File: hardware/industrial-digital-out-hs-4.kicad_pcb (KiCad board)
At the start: 2 copper layers, 40 x 40 mm, 40 parts, among them P1 CON-SENSOR, P2 Digital Output, P3 Debug, P4 Boot, Q1 FDS8449, U1 XMC1100, U2 VN7140AS, U3 VN7140AS, U4 VN7140AS, U5 VN7140AS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

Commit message: updated pcb design
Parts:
- moved R1 93.2 mm to (149.5, 88.3), turned to 90 degrees
- moved RP1 89.6 mm to (152.9, 88.2)
- moved C2 86.9 mm to (131.6, 77.9), turned to 180 degrees
- moved R2 85.6 mm to (143.5, 88.3), turned to 90 degrees
- moved RP4 82.3 mm to (146.9, 88.2)
- moved D5 81.9 mm to (150.8, 75.0), turned to 270 degrees
- moved P3 81.6 mm to (124.0, 85.2)
- moved RP2 81.0 mm to (131.6, 79.6), turned to 90 degrees
- moved R6 79.6 mm to (141.4, 94.6), turned to 90 degrees
- moved R7 77.0 mm to (141.4, 91.7), turned to 90 degrees
- moved D6 76.9 mm to (120.1, 91.6), turned to 270 degrees
- moved RP5 76.8 mm to (139.1, 88.2)
- moved RP3 76.5 mm to (148.4, 79.2), turned to 180 degrees
- moved D4 75.4 mm to (149.2, 75.0), turned to 270 degrees
- moved C3 74.1 mm to (139.4, 79.0)
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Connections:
- RP1 pad 1: OUT4 -> MSense4
- RP1 pad 4: MSense4 -> OUT4
- RP1 pad 5: Net-(R1-Pad1) -> Net-(RP1-Pad5)
- RP1 pad 8: Net-(RP1-Pad8) -> Net-(R1-Pad1)
- RP4 pad 1: OUT3 -> MSense3
- RP4 pad 4: MSense3 -> OUT3
- RP4 pad 5: Net-(R2-Pad1) -> Net-(RP4-Pad5)
- RP4 pad 8: Net-(RP4-Pad8) -> Net-(R2-Pad1)
- RP5 pad 1: OUT2 -> MSense2
- RP5 pad 4: MSense2 -> OUT2
- RP5 pad 5: Net-(R3-Pad1) -> Net-(RP5-Pad5)
- RP5 pad 8: Net-(RP5-Pad8) -> Net-(R3-Pad1)
- RP6 pad 1: OUT1 -> MSense1
- RP6 pad 4: MSense1 -> OUT1
- RP6 pad 5: Net-(R4-Pad1) -> Net-(RP6-Pad5)
- RP6 pad 8: Net-(RP6-Pad8) -> Net-(R4-Pad1)
- U1 pad 11: Net-(P4-Pad2) -> (no net)
- U1 pad 12: Net-(R5-Pad1) -> Net-(P4-Pad2)
- U1 pad 15: OUT4 -> OUT2
- U1 pad 17: OUT2 -> OUT4
- U1 pad 2: (no net) -> Net-(R5-Pad1)
- U1 pad 5: MSense2 -> VSense2
- U1 pad 6: MSense1 -> MSense2
- U1 pad 7: VSense2 -> MSense1
- U2 pad 1: Net-(RP1-Pad8) -> Net-(RP1-Pad5)
- U3 pad 1: Net-(RP4-Pad8) -> Net-(RP4-Pad5)
- U4 pad 1: Net-(RP5-Pad8) -> Net-(RP5-Pad5)
- U5 pad 1: Net-(RP6-Pad8) -> Net-(RP6-Pad5)
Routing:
- net 3V3: track 0.00 -> 98.5 mm
- net MSense4: track 0.00 -> 34.0 mm, vias 0 -> 2
- net VSense2: track 0.00 -> 33.4 mm, vias 0 -> 2
- net GND: track 0.00 -> 33.4 mm, vias 9 -> 32
- net OUT4: track 0.00 -> 31.5 mm
- net MSense3: track 0.00 -> 28.8 mm, vias 0 -> 2
- net OUT3: track 0.00 -> 26.0 mm
- net LED3: track 0.00 -> 25.0 mm
- net LED2: track 0.00 -> 23.4 mm
- net LED1: track 0.00 -> 22.5 mm
- net MSense2: track 0.00 -> 22.4 mm, vias 0 -> 2
- net LED0: track 0.00 -> 21.5 mm
- net VSense1: track 0.00 -> 20.9 mm, vias 0 -> 2
- net OUT2: track 0.00 -> 18.7 mm
- net MSense1: track 0.00 -> 16.8 mm, vias 0 -> 2
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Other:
- rule trace_min: 0.1 -> 0.15
- board text added: "0"
- board text added: "1"
- board text added: "2"
- board text added: "3"
- board text added: "Status"

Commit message: first finished prototype design
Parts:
- added Fiducial_Mark: VAL**, kicad-libraries:Fiducial_Mark, F.Cu at (155.0, 81.0)
- added Fiducial_Mark: VAL**, kicad-libraries:Fiducial_Mark, F.Cu at (120.0, 87.0)
- added Fiducial_Mark: VAL**, kicad-libraries:Fiducial_Mark, F.Cu at (155.0, 105.0)
- added Fiducial_Mark: VAL**, kicad-libraries:Fiducial_Mark, F.Cu at (142.5, 86.5)
- added Fiducial_Mark: VAL**, kicad-libraries:Fiducial_Mark, F.Cu at (125.5, 111.0)
- added G***: LOGO, kicad-libraries:Logo_CoMCU, B.Cu at (145.0, 93.0)
- added G***: LOGO, kicad-libraries:Logo_31x31, F.Cu at (144.4, 82.2)
- added VAL: WEEE_7mm, kicad-libraries:WEEE_7mm, B.Cu at (138.0, 93.0)
- added VAL: CE_5mm, kicad-libraries:CE_5mm, B.Cu at (131.5, 93.0)
- moved C1 0.71 mm to (139.8, 81.2)
- moved C2 0.71 mm to (132.1, 78.4)
- moved C3 0.71 mm to (139.9, 79.5)
- moved C4 0.71 mm to (121.9, 82.2)
- moved D1 0.71 mm to (129.5, 75.5)
- moved D2 0.71 mm to (146.5, 75.5)
- moved D3 0.71 mm to (148.1, 75.5)
- moved D4 0.71 mm to (149.7, 75.5)
- moved D5 0.71 mm to (151.3, 75.5)
- moved D6 0.71 mm to (120.6, 92.1)
- moved P1 0.71 mm to (138.0, 73.0)
- moved P2 0.71 mm to (138.0, 104.9)
- moved P3 0.71 mm to (124.5, 85.7)
- moved Q1 0.71 mm to (124.1, 94.9)
- moved R1 0.71 mm to (150.0, 88.8)
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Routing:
- net GND: track 33.4 -> 34.9 mm
- net VSense1: track 20.9 -> 22.2 mm
- net Net-(P4-Pad2): track 2.54 -> 3.05 mm
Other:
- net class Default: clearance 0.2 -> 0.19
- rule trace_clearance: 0.2 -> 0.19
- board text added: "1+2"
- board text added: "3+4"
- board text added: "4"
- board text added: "ANPASSEN!"
- board text added: "GND"
- board text added: "Industrial Digital Out HS 4"
- board text added: "OUT"
- board text added: "VCC"
- board text added: "max. 26VDC"
- board text added: "max. 4 x ?A"
- board text added: "tinkerforge.com"

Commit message: drc check
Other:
- net class Default: clearance 0.19 -> 0.149
- rule pad_to_mask_clearance: 0.051 -> 0
- rule trace_clearance: 0.19 -> 0.149
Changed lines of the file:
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@@
     (user_trace_width 2)
     (user_trace_width 3)
-    (trace_clearance 0.19)
+    (trace_clearance 0.149)
     (zone_clearance 0.2)
     (zone_45_only no)
@@
     (pad_size 1.4 1.4)
     (pad_drill 0.6)
-    (pad_to_mask_clearance 0.051)
-    (solder_mask_min_width 0.25)
+    (pad_to_mask_clearance 0)
     (aux_axis_origin 118 73)
     (grid_origin 118 73)
@@
     (pcbplotparams
       (layerselection 0x010fc_ffffffff)
-      (usegerberextensions false)
+      (usegerberextensions true)
       (usegerberattributes false)
       (usegerberadvancedattributes false)
@@
       (plotinvisibletext false)
       (padsonsilk false)
-      (subtractmaskfromsilk false)
+      (subtractmaskfromsilk true)
       (outputformat 1)
       (mirror false)
-      (drillshape 1)
+      (drillshape 0)
       (scaleselection 1)
-      (outputdirectory ""))
+      (outputdirectory "proto/"))
   )
   (net 0 "")
@@
   (net 52 "Net-(RP5-Pad5)")
   (net_class Default "Dies ist die voreingestellte Netzklasse."
-    (clearance 0.19)
+    (clearance 0.149)
     (trace_width 0.25)
     (via_dia 0.8)
@@
       (pts
         (xy 141.6 102.7) (xy 139.2 102.7) (xy 138 103.6) (xy 138 112.55) (xy 123.5 112.55)
-        (xy 123.5 107.4) (xy 134.7 107.4) (xy 134.7 103.5) (xy 135.2 91.8) (xy 141.6 91.8)
+        (xy 123.5 107.4) (xy 134.7 107.4) (xy 134.7 103.5) (xy 134.7 91.8) (xy 141.6 91.8)
       )
     )
@@
     (polygon
       (pts
-        (xy 149.2 91.8) (xy 155.6 91.8) (xy 155.6 102.7) (xy 153.2 102.7) (xy 152.3 103.6)
+        (xy 148.7 91.8) (xy 155.6 91.8) (xy 155.6 102.7) (xy 153.2 102.7) (xy 152.3 103.6)
         (xy 152.3 107) (xy 148.7 107) (xy 148.7 103.5)
       )

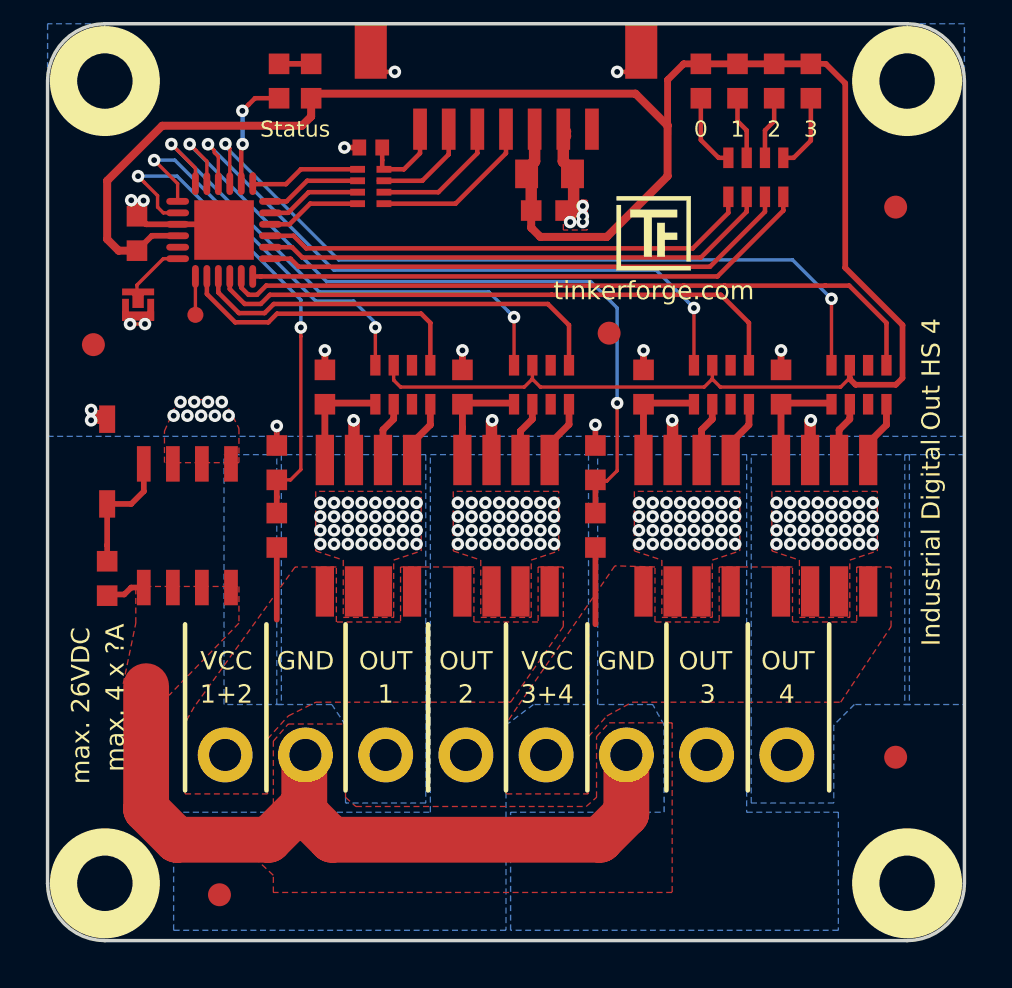
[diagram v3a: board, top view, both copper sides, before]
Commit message: changed out pins to enable pwm, changed pcb design, plotted gerber files for prototype
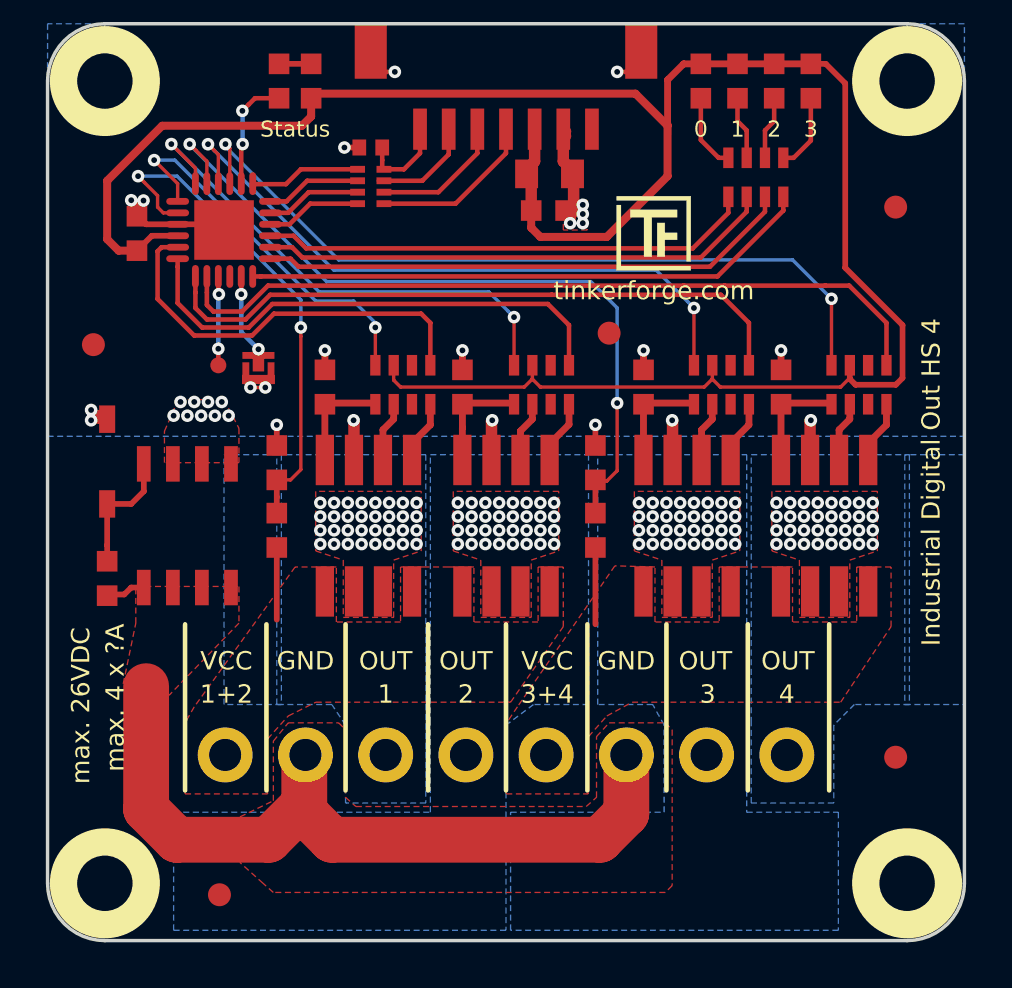
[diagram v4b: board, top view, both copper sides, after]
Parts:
- moved P4 5.94 mm to (127.2, 88.0)
- moved P3 2.42 mm to (125.5, 87.9)
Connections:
- P1 pad 1: (no net) -> Net-(P1-Pad1)
- R6 pad 2: VSense2 -> VSense1
- R7 pad 1: VSense2 -> VSense1
- R8 pad 2: VSense1 -> VSense0
- R9 pad 1: VSense1 -> VSense0
- RP1 pad 1: MSense4 -> MSense3
- RP1 pad 3: (no net) -> Net-(RP1-Pad3)
- RP1 pad 4: OUT4 -> OUT3
- RP1 pad 6: (no net) -> Net-(RP1-Pad6)
- RP4 pad 1: MSense3 -> MSense2
- RP4 pad 3: (no net) -> Net-(RP4-Pad3)
- RP4 pad 4: OUT3 -> OUT2
- RP4 pad 6: (no net) -> Net-(RP4-Pad6)
- RP5 pad 1: MSense2 -> MSense1
- RP5 pad 3: (no net) -> Net-(RP5-Pad3)
- RP5 pad 4: OUT2 -> OUT1
- RP5 pad 6: (no net) -> Net-(RP5-Pad6)
- RP6 pad 1: MSense1 -> MSense0
- RP6 pad 3: (no net) -> Net-(RP6-Pad3)
- RP6 pad 4: OUT1 -> OUT0
- RP6 pad 6: (no net) -> Net-(RP6-Pad6)
- U1 pad 11: (no net) -> OUT0
- U1 pad 12: Net-(P4-Pad2) -> OUT1
- U1 pad 13: Net-(P3-Pad1) -> OUT2
- U1 pad 14: OUT1 -> OUT3
- U1 pad 15: OUT2 -> Net-(P3-Pad1)
- U1 pad 16: OUT3 -> Net-(U1-Pad16)
- U1 pad 17: OUT4 -> Net-(P4-Pad2)
- U1 pad 3: MSense4 -> MSense3
- U1 pad 4: MSense3 -> MSense2
- U1 pad 5: VSense2 -> VSense1
- U1 pad 6: MSense2 -> MSense1
- U1 pad 7: MSense1 -> MSense0
- U1 pad 8: VSense1 -> VSense0
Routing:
- net MSense4: track 34.0 -> 0.00 mm, vias 2 -> 0
- net VSense2: track 33.4 -> 0.00 mm, vias 2 -> 0
- net OUT4: track 31.5 -> 0.00 mm
- net VSense0: track 0.00 -> 22.2 mm, vias 0 -> 2
- net OUT0: track 0.00 -> 18.0 mm
- net MSense0: track 0.00 -> 16.7 mm, vias 0 -> 2
- net VSense1: track 22.2 -> 33.4 mm
- net OUT2: track 18.7 -> 28.6 mm
- net OUT1: track 13.2 -> 22.1 mm
- net OUT3: track 26.0 -> 34.1 mm
- net MSense2: track 22.4 -> 28.6 mm
- net MSense1: track 16.7 -> 22.4 mm
- net MSense3: track 28.6 -> 34.0 mm
- net Net-(P3-Pad1): track 1.67 -> 3.94 mm, vias 0 -> 2
- net Net-(P4-Pad2): track 3.05 -> 4.11 mm, vias 0 -> 2
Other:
- board text added: "MAX A ANPASSEN!"
- board text removed: "ANPASSEN!"
